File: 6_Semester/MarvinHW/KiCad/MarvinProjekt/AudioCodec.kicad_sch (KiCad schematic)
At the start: 51 parts, among them U2 ES8388, U3 MP1720

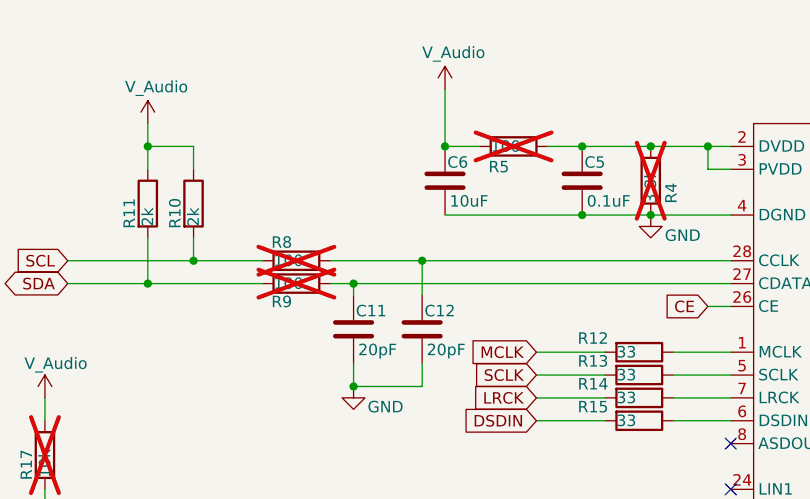
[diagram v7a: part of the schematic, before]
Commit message: change dnp from yes to no
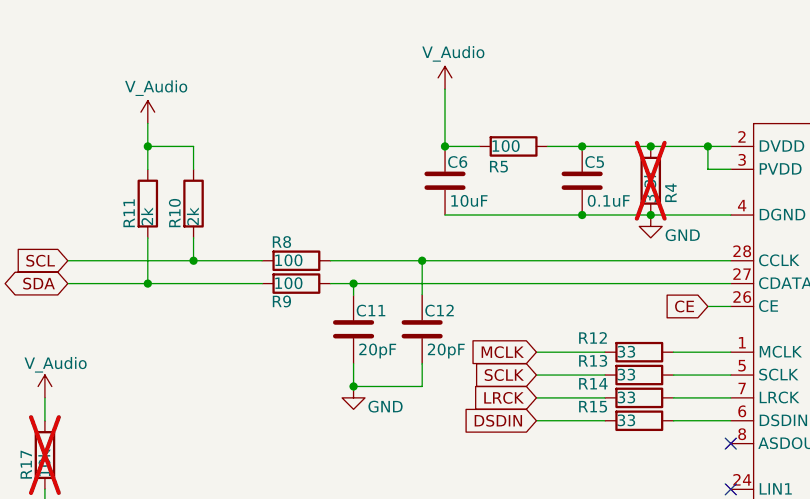
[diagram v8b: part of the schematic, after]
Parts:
- R5, R8, R9: now fitted
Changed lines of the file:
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@@
 		(in_bom yes)
 		(on_board yes)
-		(dnp yes)
+		(dnp no)
 		(property "Reference" "R9"
 			(at 45.466 43.942 90)
@@
 		(in_bom yes)
 		(on_board yes)
-		(dnp yes)
+		(dnp no)
 		(property "Reference" "R8"
 			(at 45.466 37.338 90)
@@
 		(in_bom yes)
 		(on_board yes)
-		(dnp yes)
+		(dnp no)
 		(property "Reference" "R5"
 			(at 69.596 28.956 90)
